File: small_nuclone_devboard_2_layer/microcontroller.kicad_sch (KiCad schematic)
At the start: 1 part

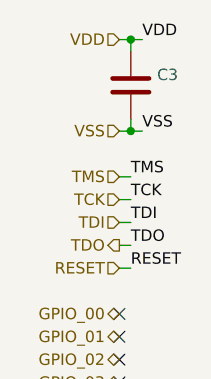
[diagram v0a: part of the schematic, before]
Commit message: small schematic changes and updated versionnumber
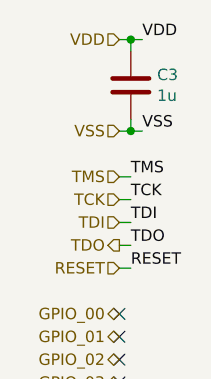
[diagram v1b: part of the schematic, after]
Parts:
- C3: value (none) -> 1u; footprint (none) -> SquantorRcl:C_0402
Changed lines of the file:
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@@
       (effects (font (size 1.27 1.27)) (justify left))
     )
-    (property "Value" "" (id 1) (at 28.321 29.083 0)
+    (property "Value" "1u" (id 1) (at 28.321 29.083 0)
       (effects (font (size 1.27 1.27)) (justify left))
     )
-    (property "Footprint" "" (id 2) (at 26.3652 31.75 0)
+    (property "Footprint" "SquantorRcl:C_0402" (id 2) (at 26.3652 31.75 0)
       (effects (font (size 1.27 1.27)) hide)
     )

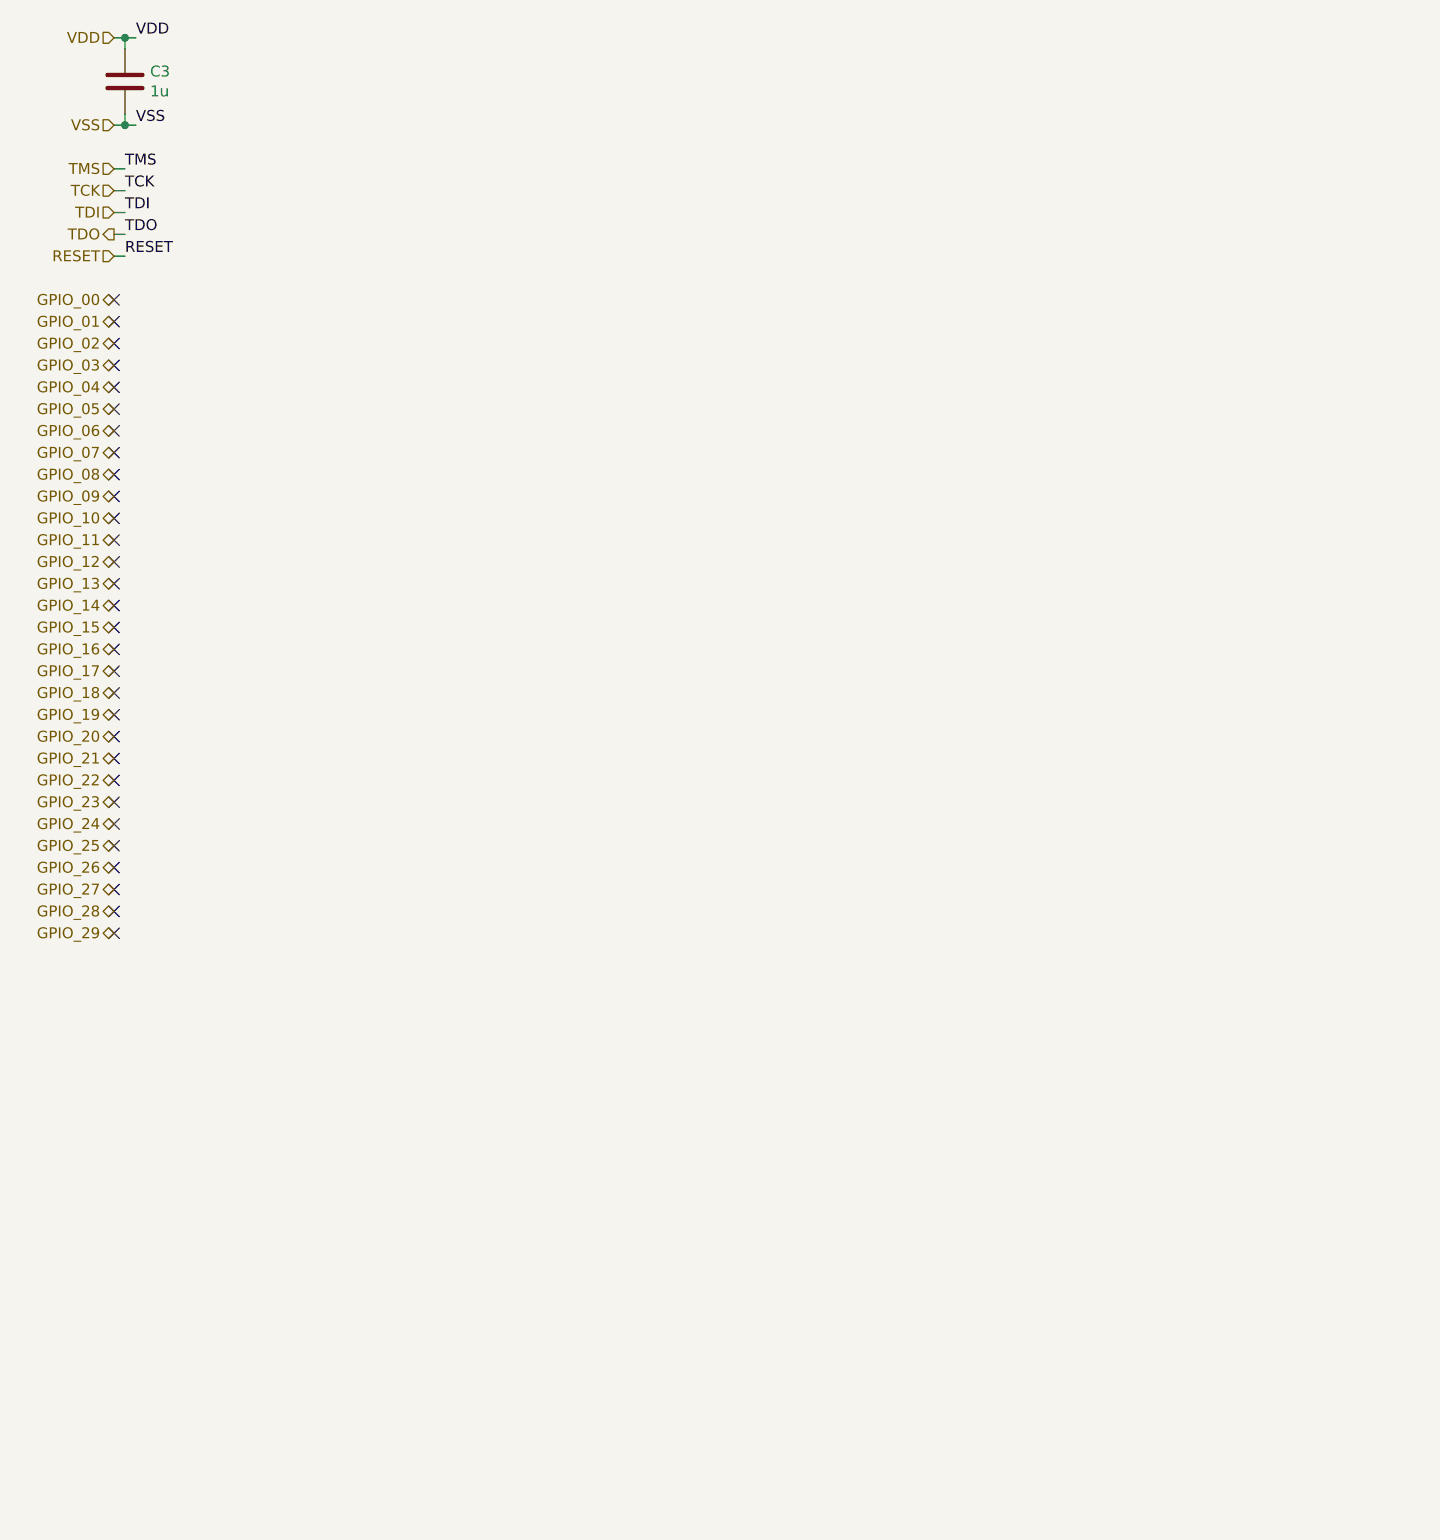
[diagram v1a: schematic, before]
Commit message: switched testpoints to test connector, changed via sizes
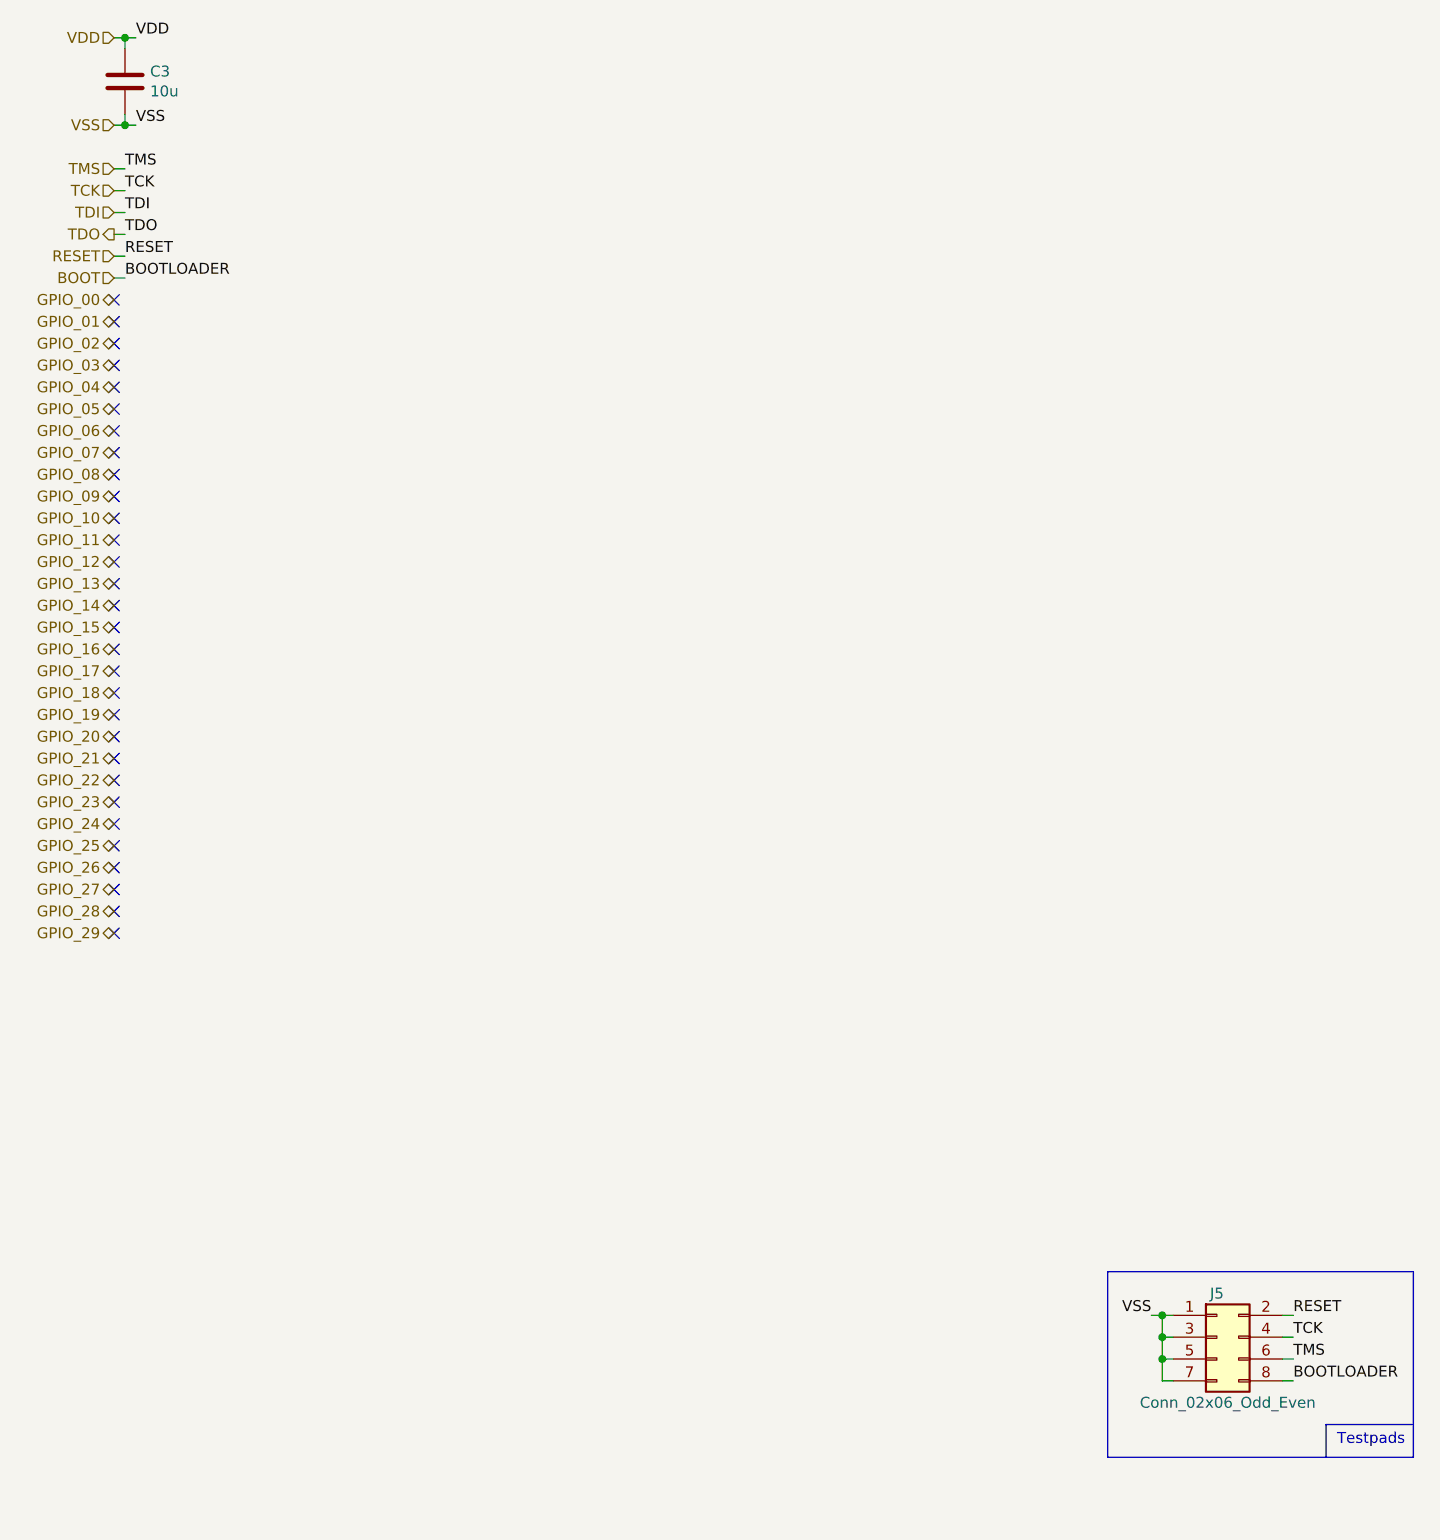
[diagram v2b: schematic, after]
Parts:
- added J5: Conn_02x06_Odd_Even, SquantorConnectors:Header-0127-2X04-H006, symbol Connector_Generic:Conn_02x04_Odd_Even
- C3: value 1u -> 10u; footprint SquantorRcl:C_0402 -> SquantorRcl:C_0603
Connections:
- net RESET: now also J5.2 (Pin_2)
- net TCK: now also J5.4 (Pin_4)
- net TMS: now also J5.6 (Pin_6)
- net VSS: now also J5.1 (Pin_1), J5.3 (Pin_3), J5.5 (Pin_5), J5.7 (Pin_7)
- new net BOOT: J5.8 (Pin_8)
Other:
- note added: "Testpads"
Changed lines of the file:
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@@
 (kicad_sch (version 20211123) (generator eeschema)
   (paper "A4")
+  (junction (at 146.05 171.45) (diameter 0) (color 0 0 0 0)
+  )
+  (junction (at 146.05 173.99) (diameter 0) (color 0 0 0 0)
+  )
+  (junction (at 146.05 176.53) (diameter 0) (color 0 0 0 0)
+  )
   (junction (at 25.4 33.02) (diameter 0) (color 0 0 0 0)
   )
@@
   (no_connect (at 24.13 73.66))
   (no_connect (at 24.13 109.22))
+  (wire (pts (xy 24.13 50.8) (xy 25.4 50.8))
+    (stroke (width 0) (type default) (color 0 0 0 0))
+  )
+  (wire (pts (xy 146.05 171.45) (xy 147.32 171.45))
+    (stroke (width 0) (type default) (color 0 0 0 0))
+  )
+  (polyline (pts (xy 175.26 186.69) (xy 175.26 187.96))
+    (stroke (width 0) (type default) (color 0 0 0 0))
+  )
+  (wire (pts (xy 160.02 171.45) (xy 161.29 171.45))
+    (stroke (width 0) (type default) (color 0 0 0 0))
+  )
+  (polyline (pts (xy 139.7 187.96) (xy 175.26 187.96))
+    (stroke (width 0) (type default) (color 0 0 0 0))
+  )
   (wire (pts (xy 25.4 33.02) (xy 25.4 31.75))
     (stroke (width 0) (type default) (color 0 0 0 0))
@@
     (stroke (width 0) (type default) (color 0 0 0 0))
   )
+  (wire (pts (xy 146.05 176.53) (xy 146.05 179.07))
+    (stroke (width 0) (type default) (color 0 0 0 0))
+  )
+  (polyline (pts (xy 175.26 166.37) (xy 139.7 166.37))
+    (stroke (width 0) (type default) (color 0 0 0 0))
+  )
   (wire (pts (xy 26.67 22.86) (xy 25.4 22.86))
     (stroke (width 0) (type default) (color 0 0 0 0))
   )
+  (polyline (pts (xy 139.7 166.37) (xy 139.7 187.96))
+    (stroke (width 0) (type default) (color 0 0 0 0))
+  )
+  (wire (pts (xy 160.02 179.07) (xy 161.29 179.07))
+    (stroke (width 0) (type default) (color 0 0 0 0))
+  )
+  (wire (pts (xy 146.05 173.99) (xy 146.05 176.53))
+    (stroke (width 0) (type default) (color 0 0 0 0))
+  )
+  (polyline (pts (xy 175.26 184.15) (xy 165.1 184.15))
+    (stroke (width 0) (type default) (color 0 0 0 0))
+  )
   (wire (pts (xy 25.4 45.72) (xy 24.13 45.72))
     (stroke (width 0) (type default) (color 0 0 0 0))
@@
     (stroke (width 0) (type default) (color 0 0 0 0))
   )
+  (wire (pts (xy 160.02 176.53) (xy 161.29 176.53))
+    (stroke (width 0) (type default) (color 0 0 0 0))
+  )
+  (polyline (pts (xy 175.26 186.69) (xy 175.26 166.37))
+    (stroke (width 0) (type default) (color 0 0 0 0))
+  )
   (wire (pts (xy 25.4 40.64) (xy 24.13 40.64))
     (stroke (width 0) (type default) (color 0 0 0 0))
   )
+  (wire (pts (xy 144.78 171.45) (xy 146.05 171.45))
+    (stroke (width 0) (type default) (color 0 0 0 0))
+  )
+  (wire (pts (xy 160.02 173.99) (xy 161.29 173.99))
+    (stroke (width 0) (type default) (color 0 0 0 0))
+  )
   (wire (pts (xy 24.13 48.26) (xy 25.4 48.26))
     (stroke (width 0) (type default) (color 0 0 0 0))
@@
     (stroke (width 0) (type default) (color 0 0 0 0))
   )
+  (wire (pts (xy 146.05 173.99) (xy 147.32 173.99))
+    (stroke (width 0) (type default) (color 0 0 0 0))
+  )
+  (wire (pts (xy 146.05 176.53) (xy 147.32 176.53))
+    (stroke (width 0) (type default) (color 0 0 0 0))
+  )
+  (wire (pts (xy 146.05 171.45) (xy 146.05 173.99))
+    (stroke (width 0) (type default) (color 0 0 0 0))
+  )
   (wire (pts (xy 24.13 22.86) (xy 25.4 22.86))
     (stroke (width 0) (type default) (color 0 0 0 0))
   )
+  (polyline (pts (xy 165.1 184.15) (xy 165.1 187.96))
+    (stroke (width 0) (type default) (color 0 0 0 0))
+  )
+  (wire (pts (xy 146.05 179.07) (xy 147.32 179.07))
+    (stroke (width 0) (type default) (color 0 0 0 0))
+  )
+  (text "Testpads" (at 166.37 186.69 0)
+    (effects (font (size 1.27 1.27)) (justify left bottom))
+  )
+  (label "BOOTLOADER" (at 25.4 50.8 0)
+    (effects (font (size 1.27 1.27)) (justify left bottom))
+  )
   (label "VDD" (at 26.67 22.86 0)
     (effects (font (size 1.27 1.27)) (justify left bottom))
   )
+  (label "BOOTLOADER" (at 161.29 179.07 0)
+    (effects (font (size 1.27 1.27)) (justify left bottom))
+  )
+  (label "TCK" (at 161.29 173.99 0)
+    (effects (font (size 1.27 1.27)) (justify left bottom))
+  )
   (label "VSS" (at 26.67 33.02 0)
     (effects (font (size 1.27 1.27)) (justify left bottom))
   )
+  (label "TMS" (at 161.29 176.53 0)
+    (effects (font (size 1.27 1.27)) (justify left bottom))
+  )
+  (label "VSS" (at 144.78 171.45 180)
+    (effects (font (size 1.27 1.27)) (justify right bottom))
+  )
   (label "RESET" (at 25.4 48.26 0)
     (effects (font (size 1.27 1.27)) (justify left bottom))
@@
     (effects (font (size 1.27 1.27)) (justify left bottom))
   )
+  (label "RESET" (at 161.29 171.45 0)
+    (effects (font (size 1.27 1.27)) (justify left bottom))
+  )
   (hierarchical_label "GPIO_16" (shape bidirectional) (at 24.13 93.98 180)
     (effects (font (size 1.27 1.27)) (justify right))
@@
   )
   (hierarchical_label "GPIO_15" (shape bidirectional) (at 24.13 91.44 180)
+    (effects (font (size 1.27 1.27)) (justify right))
+  )
+  (hierarchical_label "BOOT" (shape input) (at 24.13 50.8 180)
     (effects (font (size 1.27 1.27)) (justify right))
   )
@@
       (effects (font (size 1.27 1.27)) (justify left))
     )
-    (property "Value" "1u" (id 1) (at 28.321 29.083 0)
+    (property "Value" "10u" (id 1) (at 28.321 29.083 0)
       (effects (font (size 1.27 1.27)) (justify left))
     )
-    (property "Footprint" "SquantorRcl:C_0402" (id 2) (at 26.3652 31.75 0)
+    (property "Footprint" "SquantorRcl:C_0603" (id 2) (at 26.3652 31.75 0)
       (effects (font (size 1.27 1.27)) hide)
     )
@@
     (pin "2")
   )
+  (symbol (lib_id "Connector_Generic:Conn_02x04_Odd_Even") (at 152.4 173.99 0) (unit 1)
+    (in_bom yes) (on_board yes)
+    (property "Reference" "J5" (id 0) (at 152.4 168.91 0))
+    (property "Value" "Conn_02x06_Odd_Even" (id 1) (at 153.67 181.61 0))
+    (property "Footprint" "SquantorConnectors:Header-0127-2X04-H006" (id 2) (at 152.4 173.99 0)
+      (effects (font (size 1.27 1.27)) hide)
+    )
+    (property "Datasheet" "~" (id 3) (at 152.4 173.99 0)
+      (effects (font (size 1.27 1.27)) hide)
+    )
+    (pin "1")
+    (pin "2")
+    (pin "3")
+    (pin "4")
+    (pin "5")
+    (pin "6")
+    (pin "7")
+    (pin "8")
+  )
 )
